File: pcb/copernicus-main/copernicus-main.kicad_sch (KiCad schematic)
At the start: 36 parts, among them J1 Screw_Terminal_01x02, J2 USB_C_14P, SW1 PWR_BTN, SW2 ESTOP, SW3 BOOT_SW, SW4 SW_DPST, U1 STM32F303CBTx, U2 SN65HVD230, U3 USBLC6-2SC6, U5 THVD1400D, Y1 16MHz

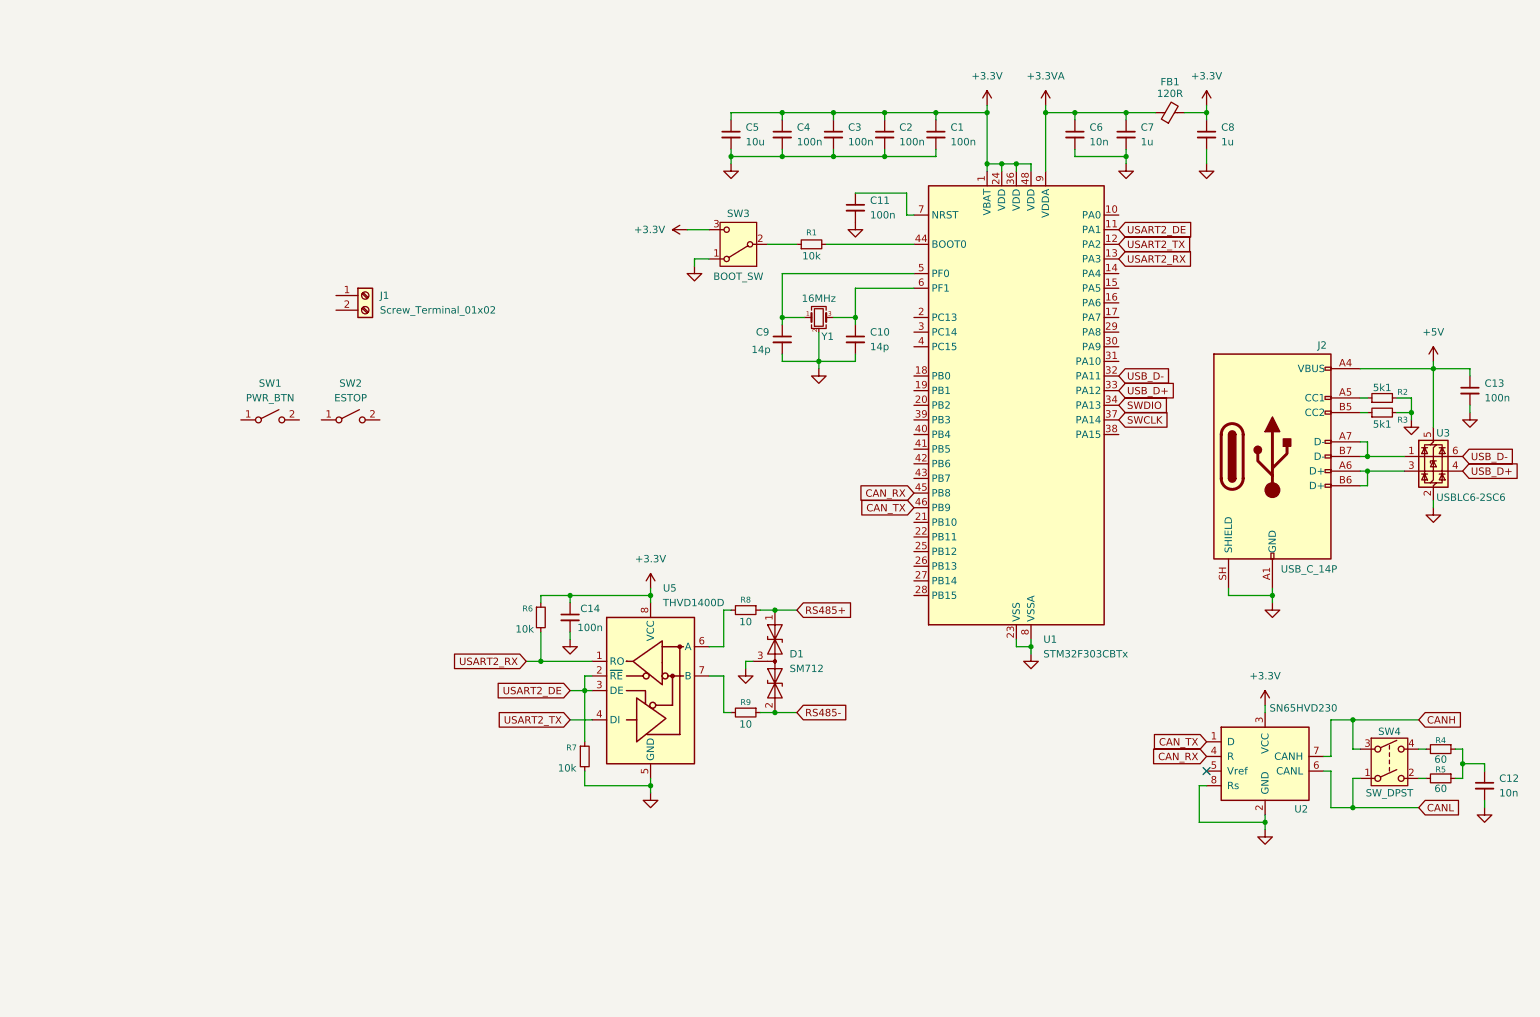
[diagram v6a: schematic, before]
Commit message: docs(pcb): added power architecture
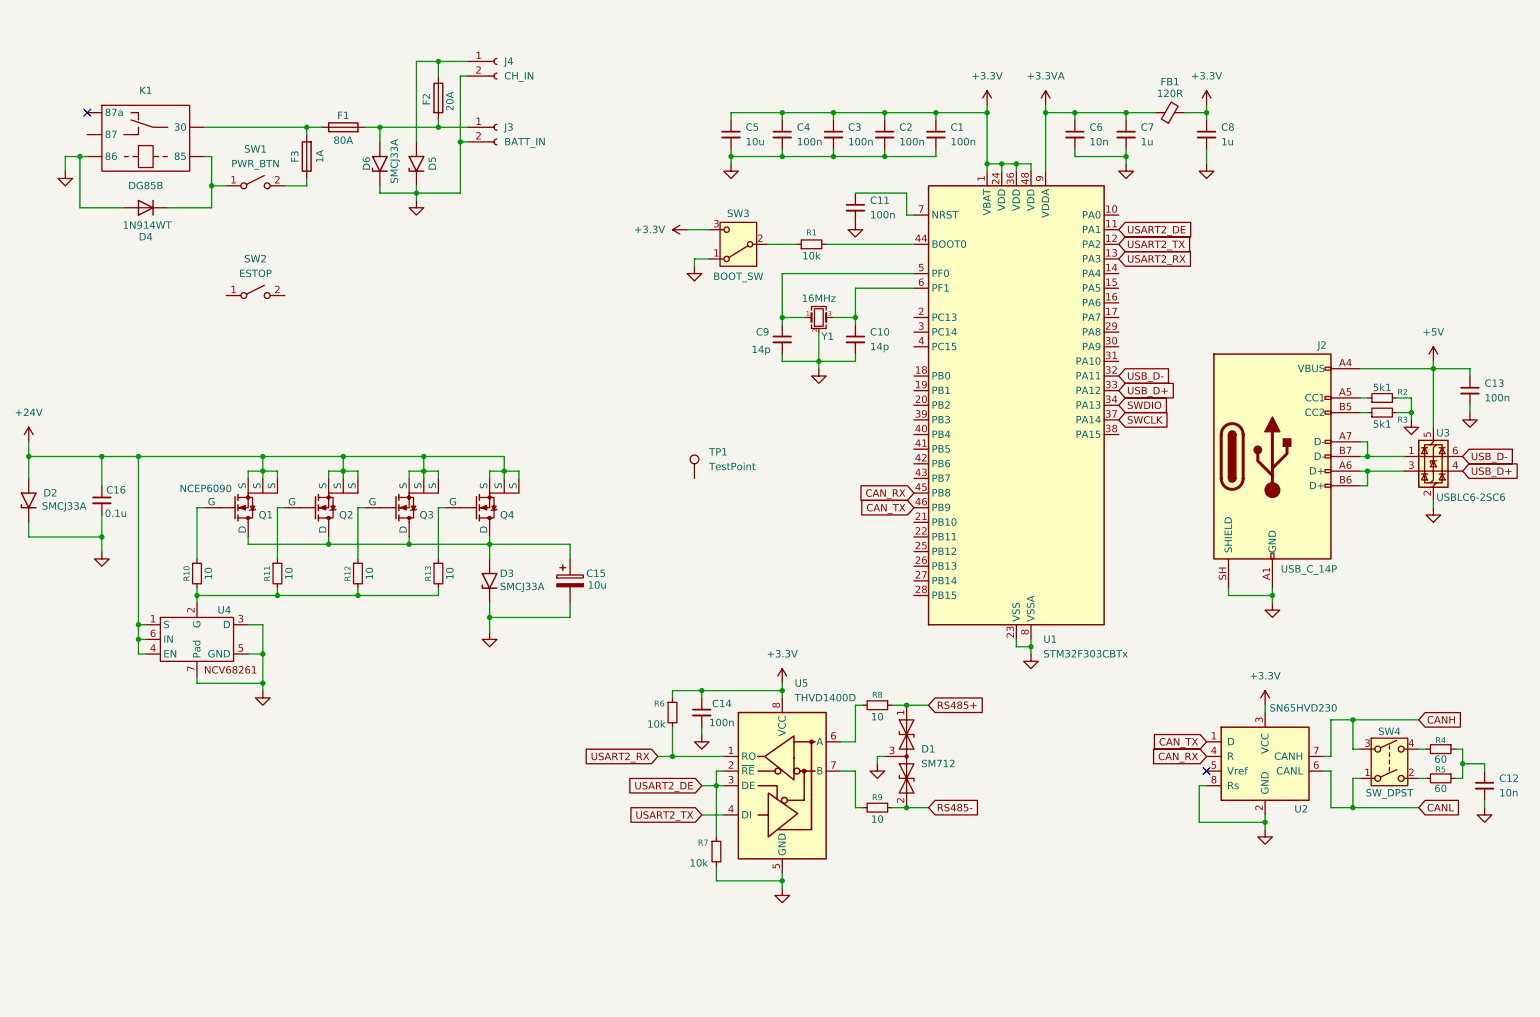
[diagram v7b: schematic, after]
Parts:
- removed J1: Screw_Terminal_01x02, symbol Connector:Screw_Terminal_01x02
- added C15: 10u, symbol Device:C_Polarized
- added C16: 0.1u, symbol Device:C_Small
- added D2, D3, D5, D6: SMCJ33A, Diode_SMD:D_SMB, symbol component-addon:SMCJ33A
- added D4: 1N914WT, Diode_SMD:D_SOD-523, symbol Diode:1N914WT
- added F1: 80A, symbol Device:Fuse
- added F2: 20A, symbol Device:Fuse
- added F3: 1A, symbol Device:Fuse
- added J3: BATT_IN, symbol Connector:Conn_01x02_Socket
- added J4: CH_IN, symbol Connector:Conn_01x02_Socket
- added K1: DG85B, symbol component-addon:DG85B
- added Q1, Q2, Q3, Q4: NCEP6090, symbol component-addon:NCEP6090AGU
- added R10, R11, R12, R13: 10, symbol Device:R_Small
- added TP1: TestPoint, symbol Connector:TestPoint
- added U4: (no value), symbol component-addon:NCV68261MTWAITBG
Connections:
- net GND: now also C15.2, C16.2, D2.1 (A1), D3.1 (A1), D4.2 (A), D5.1 (A1), D6.1 (A1), J3.2 (Pin_2), J4.2 (Pin_2), K1. (85), U4.3 (D), U4.5 (GND), U4.7 (Pad)
- net at SW1.1 (A): now also D4.1 (K), K1. (85)
- net at SW1.2 (B): now also F3.1
- new net: C15.1, D3.2 (A2), Q1.5 (D), Q2.5 (D), Q3.5 (D), Q4.5 (D)
- new net: D5.2 (A2), F2.1, J4.1 (Pin_1)
- new net: D6.2 (A2), F1.2, F2.2, J3.1 (Pin_1)
- new net: F1.1, F3.2, K1. (85)
- new net: Q1.4 (G), R10.1
- new net: R10.2, R11.2, R12.2, R13.2, U4.2 (G)
- new net: Q4.4 (G), R13.1
- new net: Q3.4 (G), R12.1
- new net: Q2.4 (G), R11.1
- new net +24V: C16.1, D2.2 (A2), Q1.1 (S), Q1.2 (S), Q1.3 (S), Q2.1 (S), Q2.2 (S), Q2.3 (S), Q3.1 (S), Q3.2 (S), Q3.3 (S), Q4.1 (S), Q4.2 (S), Q4.3 (S), U4.1 (S), U4.4 (EN), U4.6 (IN)
- no-connect marks 1 -> 2
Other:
- title: (none) -> Coppernigger control PCB
- moved on the sheet: C14, D1, R6, R7, R8, R9, SW1, SW2, U5

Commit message: docs(pcb): added buck converter
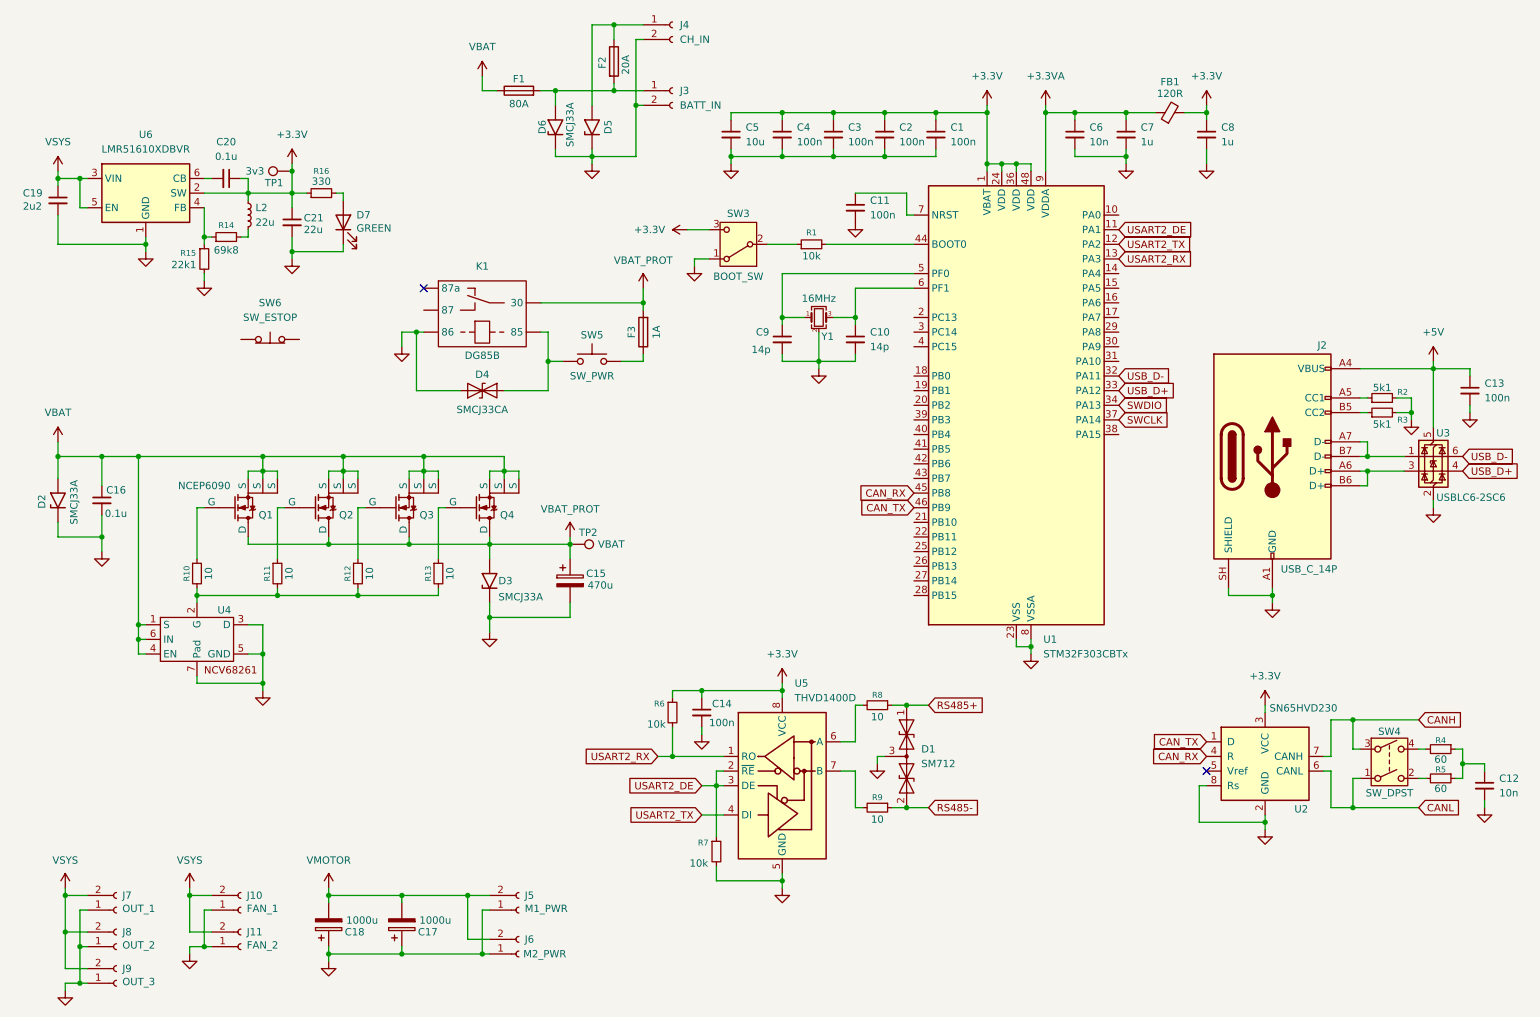
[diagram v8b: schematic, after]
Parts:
- removed D4: 1N914WT, Diode_SMD:D_SOD-523, symbol Diode:1N914WT
- removed SW1: PWR_BTN, symbol Switch:SW_SPST
- removed SW2: ESTOP, symbol Switch:SW_SPST
- added C17, C18: 1000u, symbol Device:C_Polarized
- added C19: 2u2, symbol Device:C_Small
- added C20: 0.1u, symbol Device:C_Small
- added C21: 22u, symbol Device:C_Small
- added D4: SMCJ33CA, Diode_SMD:D_SOD-323, symbol component-addon:SMCJ33CA
- added D7: GREEN, symbol Device:LED
- added J10: FAN_1, symbol Connector:Conn_01x02_Socket
- added J11: FAN_2, symbol Connector:Conn_01x02_Socket
- added J5: M1_PWR, symbol Connector:Conn_01x02_Socket
- added J6: M2_PWR, symbol Connector:Conn_01x02_Socket
- added J7: OUT_1, symbol Connector:Conn_01x02_Socket
- added J8: OUT_2, symbol Connector:Conn_01x02_Socket
- added J9: OUT_3, symbol Connector:Conn_01x02_Socket
- added L2: 22u, symbol Device:L_Small
- added R14: 69k8, symbol Device:R_Small
- added R15: 22k1, symbol Device:R_Small
- added R16: 330, symbol Device:R_Small
- added SW5: SW_PWR, symbol Switch:SW_Push
- added SW6: SW_ESTOP, symbol Switch:SW_Push_Open
- added TP2: VBAT, symbol Connector:TestPoint
- added U6: LMR51610XDBVR, Package_TO_SOT_SMD:SOT-23-6, symbol component-addon:LMR51610XDBVR
- C15: value 10u -> 470u
- TP1: value TestPoint -> 3v3
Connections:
- net +3.3V: now also TP1.1, C20.1, C21.1, L2.1, R16.1, U6.2 (SW)
- net GND: now also C17.1, C18.1, C19.2, C21.2, D4.1 (A1), D7.1 (K), J10.1 (Pin_1), J11.1 (Pin_1), J5.1 (Pin_1), J6.1 (Pin_1), J7.1 (Pin_1), J8.1 (Pin_1), J9.1 (Pin_1), R15.2, U6.1 (GND)
- net VBAT_PROT: now reaches C15.1, D3.2 (A2), Q1.5 (D), Q2.5 (D), Q3.5 (D), Q4.5 (D)
- net VBAT_PROT: now also F3.2, K1. (85), TP2.1
- net at F3.1: now also SW5.2
- net +24V renamed VBAT
- net VBAT: now also F1.1
- new net: D4.2 (A2), K1. (85), SW5.1
- new net: R14.1, R15.1, U6.4 (FB)
- new net: L2.2, R14.2
- new net: C20.2, U6.6 (CB)
- new net: D7.2 (A), R16.2
- new net VMOTOR: C17.2, C18.2, J5.2 (Pin_2), J6.2 (Pin_2)
- new net VSYS: C19.1, J10.2 (Pin_2), J11.2 (Pin_2), J7.2 (Pin_2), J8.2 (Pin_2), J9.2 (Pin_2), U6.3 (VIN), U6.5 (EN)
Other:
- moved on the sheet: D2, D5, D6, F1, F2, F3, J3, J4, K1
